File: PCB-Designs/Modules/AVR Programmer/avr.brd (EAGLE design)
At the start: 98.7 x 54.6 mm, 21 parts, among them IC1 QT9701BD, Q1 12 MHZ, X1 PN61729-S, X2 avr conn

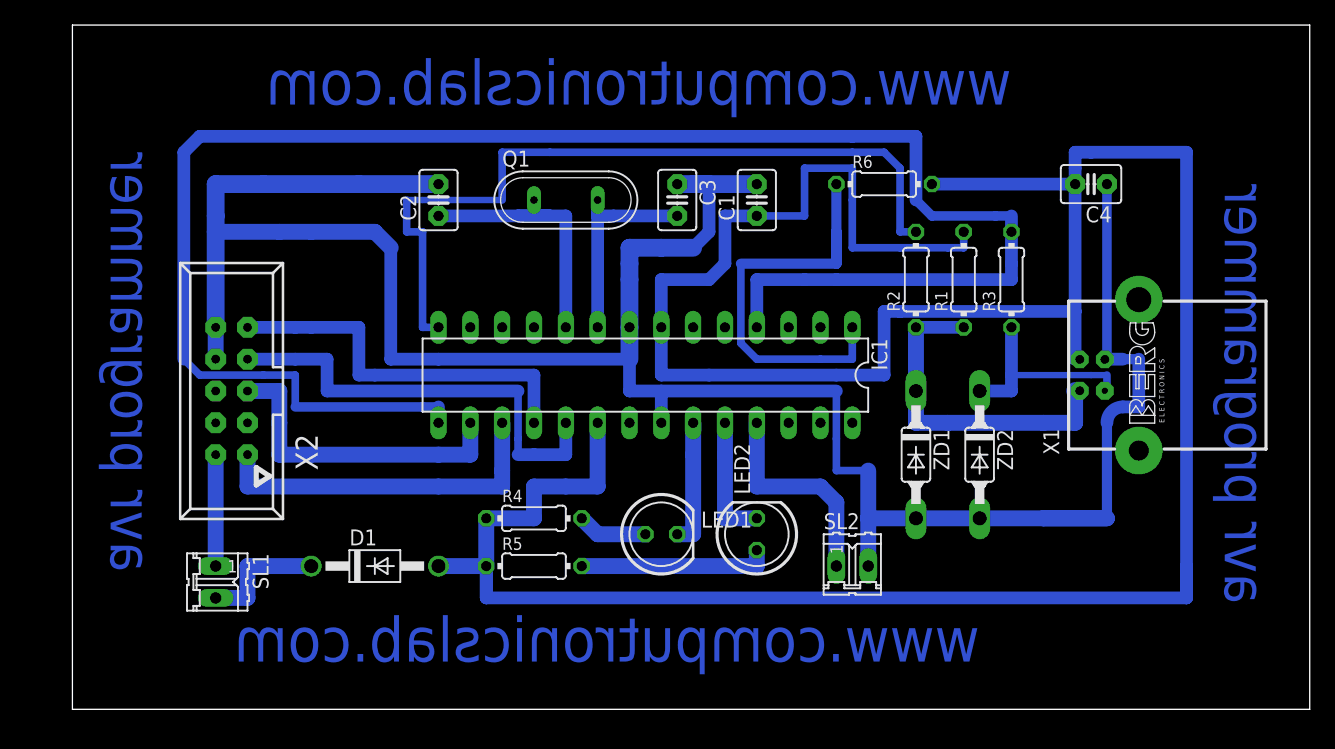
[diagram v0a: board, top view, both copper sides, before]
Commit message: 
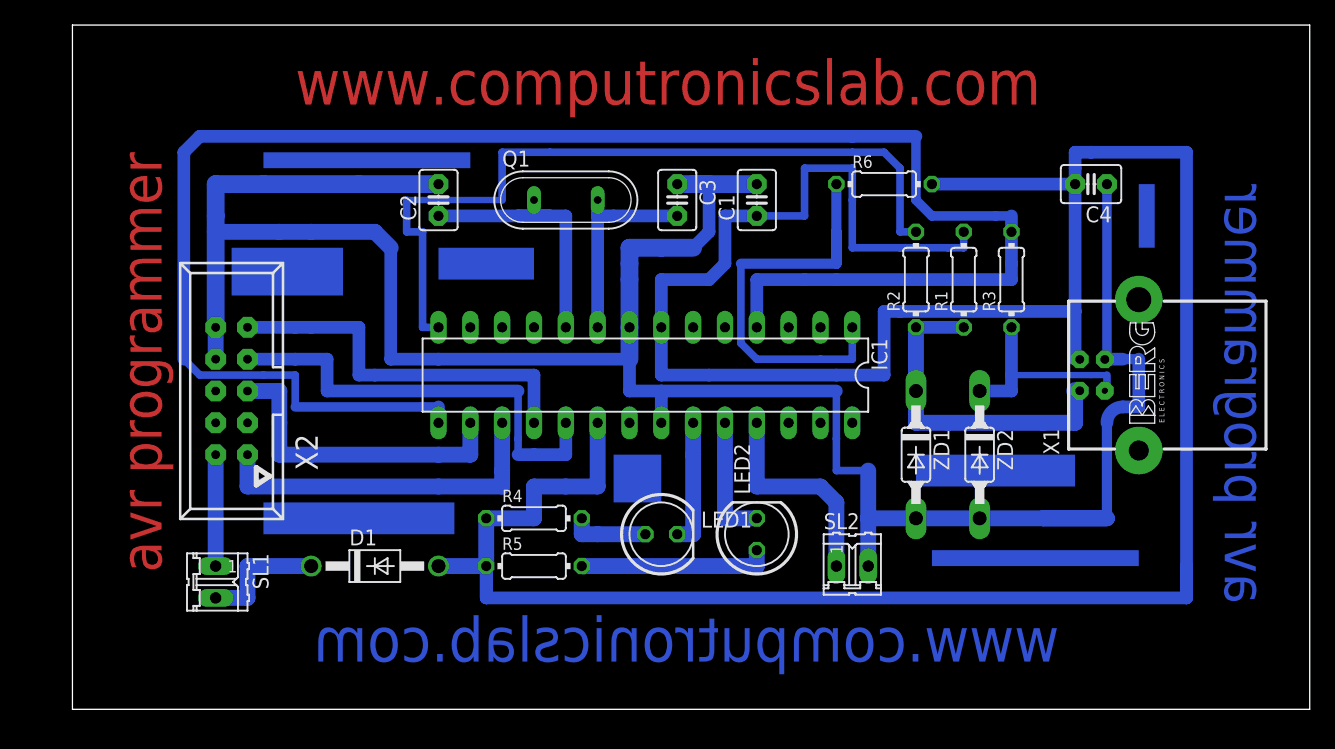
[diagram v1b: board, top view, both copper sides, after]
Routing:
- net N$21: track 5.61 -> 6.35 mm
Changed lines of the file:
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@@
 <wire x1="105.08" y1="68.57" x2="6.35" y2="68.57" width="0" layer="20"/>
 <wire x1="6.35" y1="68.57" x2="6.35" y2="13.97" width="0" layer="20"/>
-<text x="81.28" y="62.23" size="3.556" layer="16" rot="MR0">www.computronicslab.com</text>
-<text x="12.7" y="58.42" size="3.302" layer="16" rot="MR270">avr programmer</text>
-<text x="78.74" y="17.78" size="3.556" layer="16" rot="MR0">www.computronicslab.com</text>
+<text x="24.13" y="62.23" size="3.556" layer="1">www.computronicslab.com</text>
+<text x="10.16" y="58.42" size="3.302" layer="1" rot="R270">avr programmer</text>
+<text x="85.09" y="17.78" size="3.556" layer="16" rot="MR0">www.computronicslab.com</text>
 <text x="101.6" y="55.88" size="3.302" layer="16" rot="MR270">avr programmer</text>
+<rectangle x1="19.05" y1="46.99" x2="27.94" y2="50.8" layer="16"/>
+<rectangle x1="35.56" y1="48.26" x2="43.18" y2="50.8" layer="16"/>
+<rectangle x1="74.93" y1="25.4" x2="91.44" y2="26.67" layer="16"/>
+<rectangle x1="91.44" y1="50.8" x2="92.71" y2="55.88" layer="16"/>
+<rectangle x1="21.59" y1="57.15" x2="38.1" y2="58.42" layer="16"/>
+<rectangle x1="49.53" y1="30.48" x2="53.34" y2="34.29" layer="16"/>
+<rectangle x1="21.59" y1="27.94" x2="36.83" y2="30.48" layer="16"/>
+<rectangle x1="73.66" y1="31.75" x2="86.36" y2="34.29" layer="16"/>
 </plain>
 <attributes>
@@
 <wire x1="68.58" y1="59.69" x2="16.51" y2="59.69" width="1.016" layer="16"/>
 <wire x1="74.93" y1="53.34" x2="73.66" y2="54.61" width="0.762" layer="16"/>
-<wire x1="73.66" y1="54.61" x2="73.66" y2="59.69" width="1.016" layer="16"/>
+<wire x1="73.66" y1="54.61" x2="73.66" y2="59.69" width="0.762" layer="16"/>
 <wire x1="73.66" y1="59.69" x2="68.58" y2="59.69" width="1.016" layer="16"/>
 <wire x1="80.01" y1="53.34" x2="74.93" y2="53.34" width="0.762" layer="16"/>
@@
 <contactref element="R4" pad="2"/>
 <contactref element="LED1" pad="A"/>
-<wire x1="48.26" y1="27.94" x2="46.99" y2="29.21" width="1.27" layer="16"/>
+<wire x1="48.26" y1="27.94" x2="46.99" y2="27.94" width="1.27" layer="16"/>
+<wire x1="46.99" y1="27.94" x2="46.99" y2="29.21" width="1.27" layer="16"/>
 <wire x1="52.07" y1="27.94" x2="48.26" y2="27.94" width="1.27" layer="16"/>
 </signal>
